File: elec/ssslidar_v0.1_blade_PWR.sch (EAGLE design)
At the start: 22 parts, among them P1 PIN_SMD_0.8X1_RECT, P10 PIN_SMD_0.8X1_RECT, P11 PIN_SMD_1X1_RECT, P12 PIN_SMD_0.8X1_RECT, P13 PIN_SMD_0.8X1_RECT, P16 PIN_SMD_0.8X1_RECT, P17 PIN_SMD_1X1_RECT, P18 PIN_SMD_0.8X1_RECT, P2 PIN_SMD_1X1_RECT, P3 PIN_SMD_0.8X1_RECT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

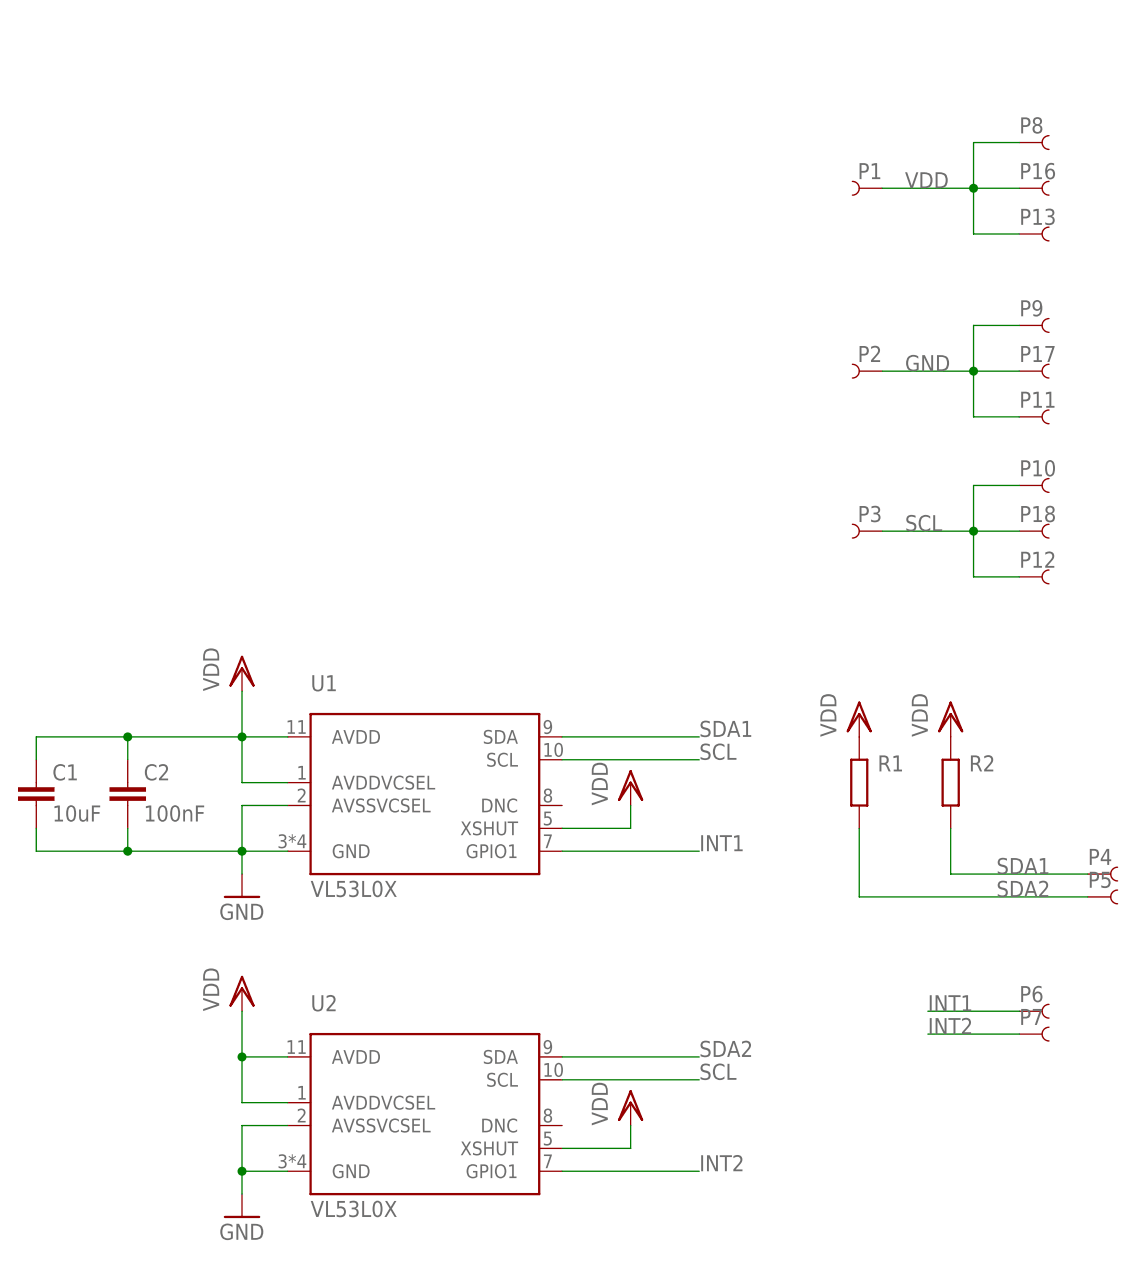
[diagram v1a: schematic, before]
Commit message: Updated blades (ready for release). Double power rail for sensors.
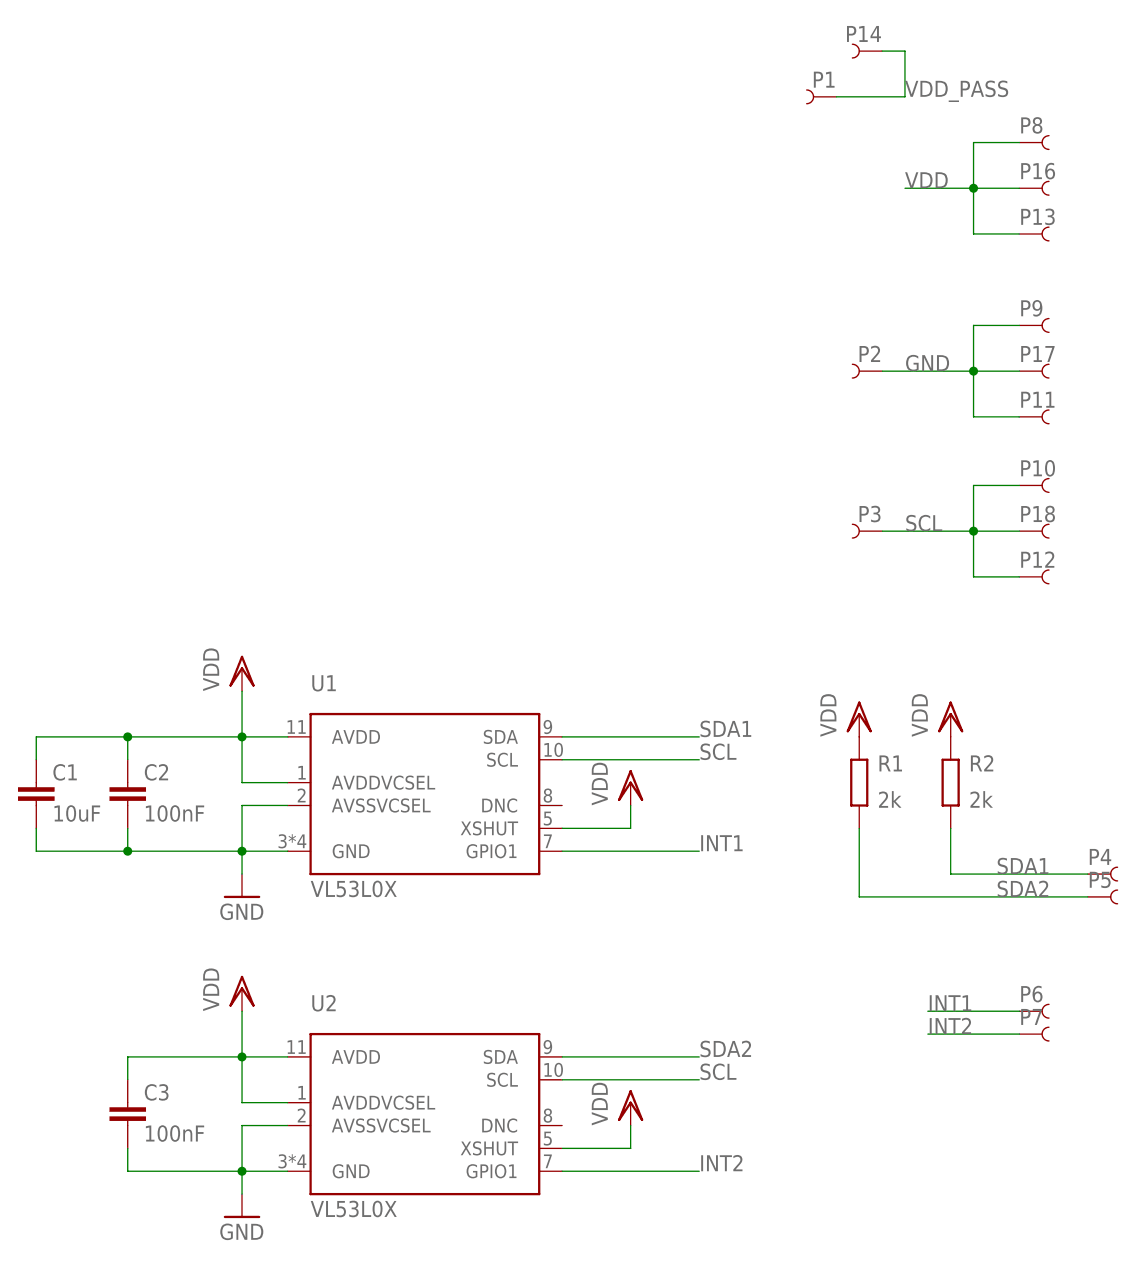
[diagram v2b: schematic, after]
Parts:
- added C3: 100nF, Xevelabs:C0402
- added P14: PIN_SMD_0.8X1_RECT, Xevelabs:PIN_SMD_0.8X1_RECT
- R1, R2: value (none) -> 2k
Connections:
- new net VDD_PASS: P1.1, P14.1
- net GND: now also C3.2
- net VDD: now also C3.1; no longer P1.1
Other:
- moved on the sheet: P1
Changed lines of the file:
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@@
 <grid distance="0.1" unitdist="inch" unit="inch" style="lines" multiple="1" display="no" altdistance="0.01" altunitdist="inch" altunit="inch"/>
 <layers>
-<layer number="1" name="Top" color="4" fill="1" visible="yes" active="no"/>
-<layer number="2" name="Route2" color="1" fill="3" visible="yes" active="no"/>
-<layer number="3" name="Route3" color="4" fill="3" visible="yes" active="no"/>
-<layer number="14" name="Route14" color="1" fill="6" visible="yes" active="no"/>
-<layer number="15" name="Route15" color="4" fill="6" visible="yes" active="no"/>
-<layer number="16" name="Bottom" color="1" fill="1" visible="yes" active="no"/>
-<layer number="17" name="Pads" color="2" fill="1" visible="yes" active="no"/>
-<layer number="18" name="Vias" color="2" fill="1" visible="yes" active="no"/>
-<layer number="19" name="Unrouted" color="6" fill="1" visible="yes" active="no"/>
-<layer number="20" name="Dimension" color="15" fill="1" visible="yes" active="no"/>
-<layer number="21" name="tPlace" color="7" fill="1" visible="yes" active="no"/>
-<layer number="22" name="bPlace" color="7" fill="1" visible="yes" active="no"/>
-<layer number="23" name="tOrigins" color="15" fill="1" visible="yes" active="no"/>
-<layer number="24" name="bOrigins" color="15" fill="1" visible="yes" active="no"/>
-<layer number="25" name="tNames" color="7" fill="1" visible="yes" active="no"/>
-<layer number="26" name="bNames" color="7" fill="1" visible="yes" active="no"/>
-<layer number="27" name="tValues" color="7" fill="1" visible="yes" active="no"/>
-<layer number="28" name="bValues" color="7" fill="1" visible="yes" active="no"/>
+<layer number="1" name="Top" color="4" fill="1" visible="no" active="no"/>
+<layer number="2" name="Route2" color="1" fill="3" visible="no" active="no"/>
+<layer number="3" name="Route3" color="4" fill="3" visible="no" active="no"/>
+<layer number="14" name="Route14" color="1" fill="6" visible="no" active="no"/>
+<layer number="15" name="Route15" color="4" fill="6" visible="no" active="no"/>
+<layer number="16" name="Bottom" color="1" fill="1" visible="no" active="no"/>
+<layer number="17" name="Pads" color="2" fill="1" visible="no" active="no"/>
+<layer number="18" name="Vias" color="2" fill="1" visible="no" active="no"/>
+<layer number="19" name="Unrouted" color="6" fill="1" visible="no" active="no"/>
+<layer number="20" name="Dimension" color="15" fill="1" visible="no" active="no"/>
+<layer number="21" name="tPlace" color="7" fill="1" visible="no" active="no"/>
+<layer number="22" name="bPlace" color="7" fill="1" visible="no" active="no"/>
+<layer number="23" name="tOrigins" color="15" fill="1" visible="no" active="no"/>
+<layer number="24" name="bOrigins" color="15" fill="1" visible="no" active="no"/>
+<layer number="25" name="tNames" color="7" fill="1" visible="no" active="no"/>
+<layer number="26" name="bNames" color="7" fill="1" visible="no" active="no"/>
+<layer number="27" name="tValues" color="7" fill="1" visible="no" active="no"/>
+<layer number="28" name="bValues" color="7" fill="1" visible="no" active="no"/>
 <layer number="29" name="tStop" color="7" fill="3" visible="no" active="no"/>
 <layer number="30" name="bStop" color="7" fill="6" visible="no" active="no"/>
@@
 <layer number="35" name="tGlue" color="7" fill="4" visible="no" active="no"/>
 <layer number="36" name="bGlue" color="7" fill="5" visible="no" active="no"/>
-<layer number="37" name="tTest" color="7" fill="1" visible="yes" active="no"/>
-<layer number="38" name="bTest" color="7" fill="1" visible="yes" active="no"/>
+<layer number="37" name="tTest" color="7" fill="1" visible="no" active="no"/>
+<layer number="38" name="bTest" color="7" fill="1" visible="no" active="no"/>
 <layer number="39" name="tKeepout" color="4" fill="11" visible="no" active="no"/>
 <layer number="40" name="bKeepout" color="1" fill="11" visible="no" active="no"/>
@@
 <layer number="44" name="Drills" color="7" fill="1" visible="no" active="no"/>
 <layer number="45" name="Holes" color="7" fill="1" visible="no" active="no"/>
-<layer number="46" name="Milling" color="3" fill="1" visible="yes" active="no"/>
-<layer number="47" name="Measures" color="7" fill="1" visible="yes" active="no"/>
-<layer number="48" name="Document" color="7" fill="1" visible="yes" active="no"/>
-<layer number="49" name="Reference" color="7" fill="1" visible="yes" active="no"/>
-<layer number="50" name="dxf" color="7" fill="1" visible="yes" active="no"/>
-<layer number="51" name="tDocu" color="7" fill="1" visible="yes" active="no"/>
-<layer number="52" name="bDocu" color="7" fill="1" visible="yes" active="no"/>
-<layer number="53" name="tGND_GNDA" color="7" fill="9" visible="yes" active="no"/>
-<layer number="54" name="bGND_GNDA" color="1" fill="9" visible="yes" active="no"/>
-<layer number="56" name="wert" color="7" fill="1" visible="yes" active="no"/>
+<layer number="46" name="Milling" color="3" fill="1" visible="no" active="no"/>
+<layer number="47" name="Measures" color="7" fill="1" visible="no" active="no"/>
+<layer number="48" name="Document" color="7" fill="1" visible="no" active="no"/>
+<layer number="49" name="Reference" color="7" fill="1" visible="no" active="no"/>
+<layer number="50" name="dxf" color="7" fill="1" visible="no" active="no"/>
+<layer number="51" name="tDocu" color="7" fill="1" visible="no" active="no"/>
+<layer number="52" name="bDocu" color="7" fill="1" visible="no" active="no"/>
+<layer number="53" name="tGND_GNDA" color="7" fill="9" visible="no" active="no"/>
+<layer number="54" name="bGND_GNDA" color="1" fill="9" visible="no" active="no"/>
+<layer number="56" name="wert" color="7" fill="1" visible="no" active="no"/>
 <layer number="90" name="Modules" color="5" fill="1" visible="yes" active="yes"/>
 <layer number="91" name="Nets" color="2" fill="1" visible="yes" active="yes"/>
@@
 <part name="P12" library="Xevelabs" deviceset="PIN" device="_SMD_0.8X1_RECT" value="PIN_SMD_0.8X1_RECT"/>
 <part name="P13" library="Xevelabs" deviceset="PIN" device="_SMD_0.8X1_RECT" value="PIN_SMD_0.8X1_RECT"/>
-<part name="R1" library="Xevelabs" deviceset="R" device="0402"/>
-<part name="R2" library="Xevelabs" deviceset="R" device="0402"/>
+<part name="R1" library="Xevelabs" deviceset="R" device="0402" value="2k"/>
+<part name="R2" library="Xevelabs" deviceset="R" device="0402" value="2k"/>
 <part name="VDD5" library="supply1" deviceset="VDD" device=""/>
 <part name="VDD6" library="supply1" deviceset="VDD" device=""/>
+<part name="P14" library="Xevelabs" deviceset="PIN" device="_SMD_0.8X1_RECT" value="PIN_SMD_0.8X1_RECT"/>
+<part name="C3" library="Xevelabs" deviceset="C" device="0402" value="100nF"/>
 </parts>
 <sheets>
@@
 <instance part="VDD3" gate="G$1" x="27.94" y="30.48"/>
 <instance part="VDD4" gate="G$1" x="71.12" y="17.78"/>
-<instance part="P1" gate="G$1" x="99.06" y="119.38" rot="MR0"/>
+<instance part="P1" gate="G$1" x="93.98" y="129.54" rot="MR0"/>
 <instance part="P2" gate="G$1" x="99.06" y="99.06" rot="MR0"/>
 <instance part="P3" gate="G$1" x="99.06" y="81.28" rot="MR0"/>
@@
 <instance part="VDD5" gate="G$1" x="96.52" y="60.96"/>
 <instance part="VDD6" gate="G$1" x="106.68" y="60.96"/>
+<instance part="P14" gate="G$1" x="99.06" y="134.62" rot="MR0"/>
+<instance part="C3" gate="G$1" x="15.24" y="15.24"/>
 </instances>
 <busses>
@@
 <wire x1="27.94" y1="17.78" x2="27.94" y2="22.86" width="0.1524" layer="91"/>
 <junction x="27.94" y="22.86"/>
+<pinref part="C3" gate="G$1" pin="1"/>
+<wire x1="15.24" y1="20.32" x2="15.24" y2="22.86" width="0.1524" layer="91"/>
+<wire x1="15.24" y1="22.86" x2="27.94" y2="22.86" width="0.1524" layer="91"/>
 </segment>
 <segment>
@@
 </segment>
 <segment>
-<pinref part="P1" gate="G$1" pin="1"/>
 <pinref part="P16" gate="G$1" pin="1"/>
-<wire x1="99.06" y1="119.38" x2="109.22" y2="119.38" width="0.1524" layer="91"/>
+<wire x1="101.6" y1="119.38" x2="109.22" y2="119.38" width="0.1524" layer="91"/>
 <label x="101.6" y="119.38" size="1.778" layer="95"/>
 <pinref part="P8" gate="G$1" pin="1"/>
@@
 <wire x1="27.94" y1="15.24" x2="27.94" y2="10.16" width="0.1524" layer="91"/>
 <junction x="27.94" y="10.16"/>
+<wire x1="27.94" y1="10.16" x2="15.24" y2="10.16" width="0.1524" layer="91"/>
+<pinref part="C3" gate="G$1" pin="2"/>
+<wire x1="15.24" y1="10.16" x2="15.24" y2="12.7" width="0.1524" layer="91"/>
 </segment>
 <segment>
@@
 </segment>
 </net>
+<net name="VDD_PASS" class="0">
+<segment>
+<pinref part="P1" gate="G$1" pin="1"/>
+<wire x1="93.98" y1="129.54" x2="101.6" y2="129.54" width="0.1524" layer="91"/>
+<wire x1="101.6" y1="129.54" x2="101.6" y2="134.62" width="0.1524" layer="91"/>
+<pinref part="P14" gate="G$1" pin="1"/>
+<wire x1="101.6" y1="134.62" x2="99.06" y2="134.62" width="0.1524" layer="91"/>
+<label x="101.6" y="129.54" size="1.778" layer="95"/>
+</segment>
+</net>
